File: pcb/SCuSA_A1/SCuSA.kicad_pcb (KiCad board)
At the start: 2 copper layers, 22 parts, among them J101 Header_01x02_Wurth_61300211121, J102 USB4135-GF-A, Q102 DMP2022LSS, U1 LM27762, U101 MCP73812T-420I-OT, U103 BQ297xy

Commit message: Work on battery charger
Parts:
- removed J101: Header_01x02_Wurth_61300211121, Connector_PinHeader_2.54mm:PinHeader_1x02_P2.54mm_Vertical
- added D101: 150080SS75000, LED_SMD:LED_0805_2012Metric_Pad1.15x1.40mm_HandSolder, F.Cu at (143.7, 78.4)
- added F101: 0ZCJ0110FF2E, Fuse:Fuse_1206_3216Metric_Pad1.42x1.75mm_HandSolder, F.Cu at (144.2, 75.2)
- added J105: JST_S2B-PH-K-x, Connector_JST:JST_PH_S2B-PH-K_1x02_P2.00mm_Horizontal, F.Cu at (144.2, 66.3)
- added R109: 5.1M,0603, Resistor_SMD:R_0603_1608Metric_Pad0.98x0.95mm_HandSolder, F.Cu at (139.1, 65.2)
- added R110: 5.1M,0603, Resistor_SMD:R_0603_1608Metric_Pad0.98x0.95mm_HandSolder, F.Cu at (139.1, 67.7)
- added R111: 5.1k,0603, Resistor_SMD:R_0603_1608Metric_Pad0.98x0.95mm_HandSolder, F.Cu at (139.1, 70.2)
- added R112: 5.1k,0603, Resistor_SMD:R_0603_1608Metric_Pad0.98x0.95mm_HandSolder, F.Cu at (139.1, 72.7)
- added R113: 10k,0603, Resistor_SMD:R_0603_1608Metric_Pad0.98x0.95mm_HandSolder, F.Cu at (139.1, 75.2)
- added U104: TLV803EA30DBZR, Package_TO_SOT_SMD:SOT-23, F.Cu at (149.7, 75.8)
- Q102: value DMP2022LSS -> DMN2041LSD
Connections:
- C1 pad 1: VBat -> /VBat_SW
- C104 pad 1: VBat -> /VBat
- J102 pad A5: unconnected-(J102-CC1-PadA5) -> Net-(J102-CC1)
- J102 pad A9: /VBus -> Net-(F101-Pad1)
- J102 pad B5: unconnected-(J102-CC2-PadB5) -> Net-(J102-CC2)
- J102 pad B9: /VBus -> Net-(F101-Pad1)
- R102 pad 1: VBat -> /VBat
- U1 pad 12: unconnected-(U1-EN+-Pad12) -> Net-(JP102-B)
- U1 pad 3: VBat -> /VBat_SW
- U1 pad 8: unconnected-(U1-EN--Pad8) -> Net-(JP101-B)
- U101 pad 3: VBat -> /VBat
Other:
- board outline added: 40 x 30 mm

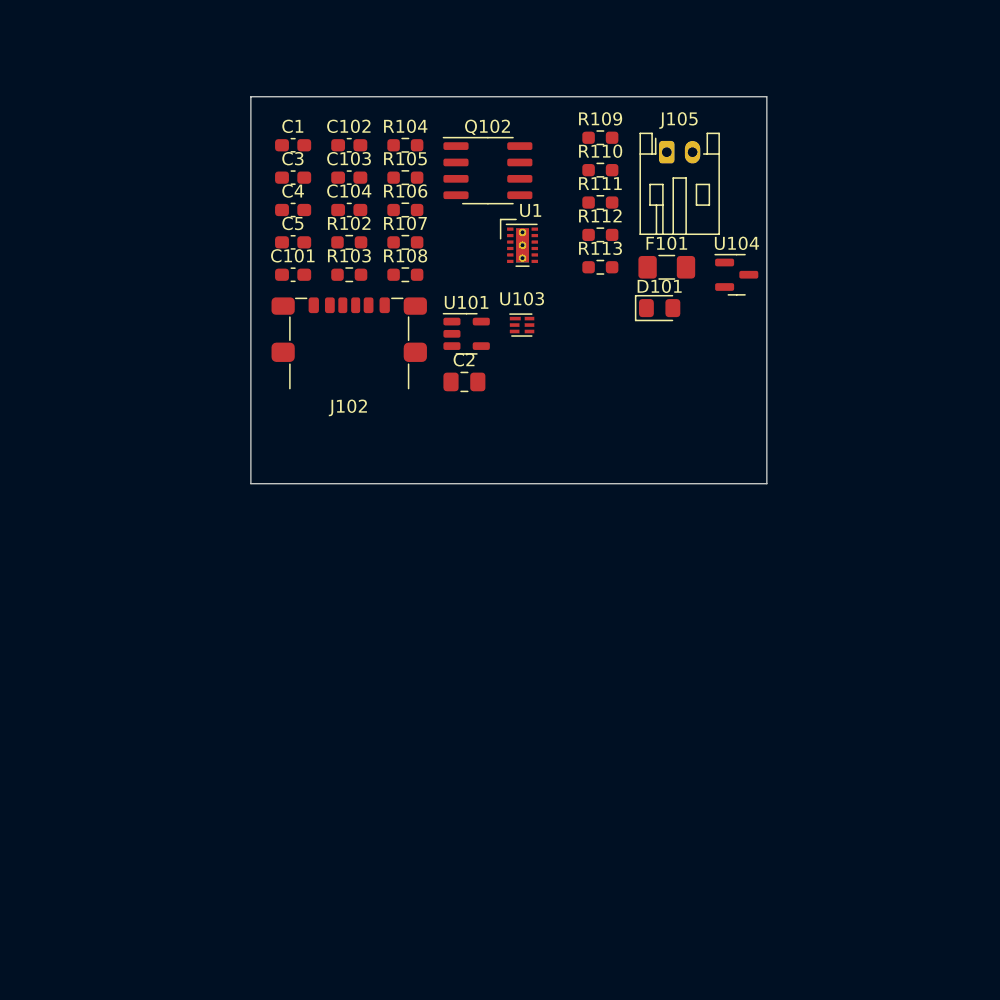
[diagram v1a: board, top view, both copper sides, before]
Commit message: Add trimpot, bindingpost
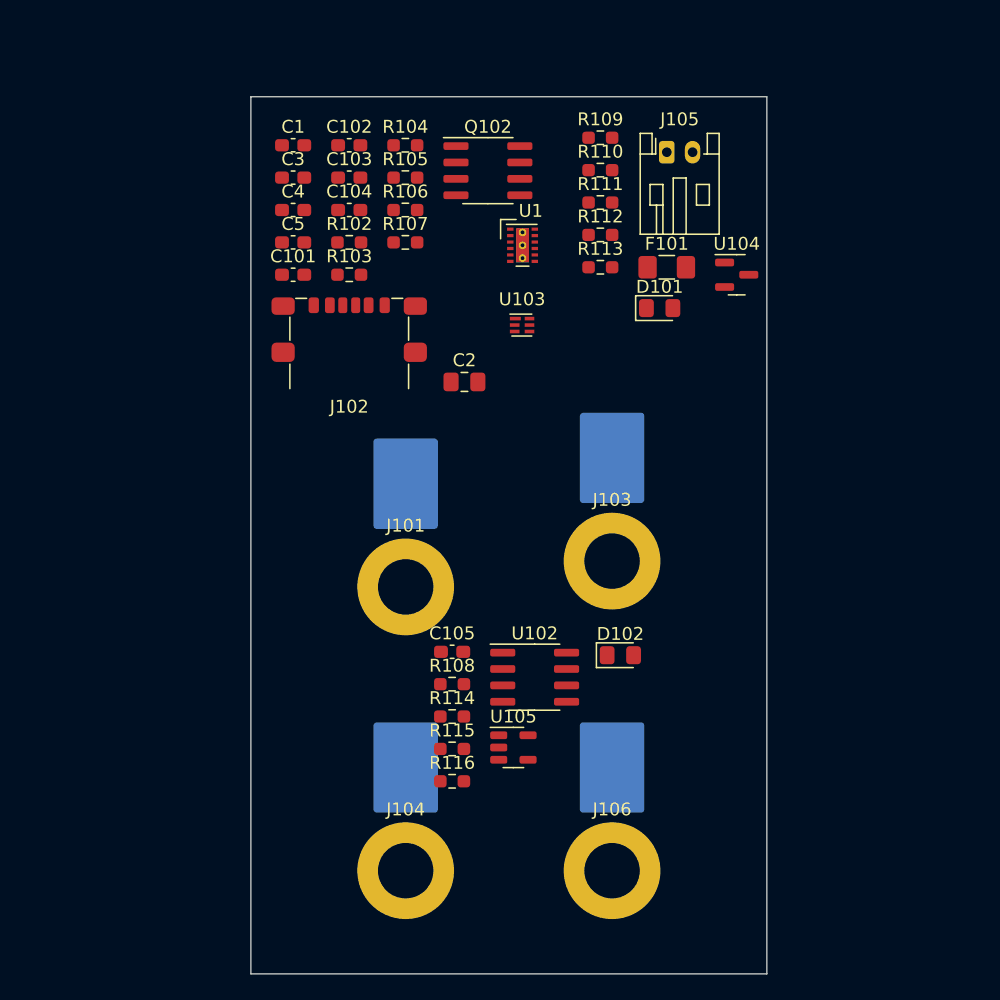
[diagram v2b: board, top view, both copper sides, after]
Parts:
- removed U101: MCP73812T-420I-OT, Package_TO_SOT_SMD:SOT-23-5
- added C105: 100nF,100V,X7R,0603, Capacitor_SMD:C_0603_1608Metric_Pad1.08x0.95mm_HandSolder, F.Cu at (127.6, 105.0)
- added D102: 150080BS75000, LED_SMD:LED_0805_2012Metric_Pad1.15x1.40mm_HandSolder, F.Cu at (140.6, 105.3)
- added J101: Binding_Post_PK4_Red, Connector_User:Binding_Post_4.3mm_M4_DIN965_Pad, F.Cu at (124.0, 100.0)
- added J103: Binding_Post_PK4_Black, Connector_User:Binding_Post_4.3mm_M4_DIN965_Pad, F.Cu at (140.0, 98.0)
- added J104: Binding_Post_PK4_Black, Connector_User:Binding_Post_4.3mm_M4_DIN965_Pad, F.Cu at (124.0, 122.0)
- added J106: Binding_Post_PK4_Red, Connector_User:Binding_Post_4.3mm_M4_DIN965_Pad, F.Cu at (140.0, 122.0)
- added R114: 470R,0603, Resistor_SMD:R_0603_1608Metric_Pad0.98x0.95mm_HandSolder, F.Cu at (127.6, 110.0)
- added R115: 0R,0603, Resistor_SMD:R_0603_1608Metric_Pad0.98x0.95mm_HandSolder, F.Cu at (127.6, 112.6)
- added R116: 0R,0603, Resistor_SMD:R_0603_1608Metric_Pad0.98x0.95mm_HandSolder, F.Cu at (127.6, 115.1)
- added U102: AD8410AWBRZ, Package_SO:SOIC-8_3.9x4.9mm_P1.27mm, F.Cu at (134.0, 107.0)
- added U105: MCP73832T-2ACI/OT, Package_TO_SOT_SMD:SOT-23-5, F.Cu at (132.3, 112.5)
- R108: value 10k,0603 -> 2k,0603
- moved R108 31.9 mm to (127.6, 107.5)
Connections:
- net Net-(U1-OUT-) renamed /-2V
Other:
- board size 40 x 30 mm -> 40 x 68 mm

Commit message: Completion of schematic (for now)
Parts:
- removed C1, C3, C4: 2.2uF,25V,X7R,0603, Capacitor_SMD:C_0603_1608Metric_Pad1.08x0.95mm_HandSolder
- removed C2: 4.7uF,25V,X7R,0805, Capacitor_SMD:C_0805_2012Metric_Pad1.18x1.45mm_HandSolder
- removed C5: 470nF,25V,X7R,0603, Capacitor_SMD:C_0603_1608Metric_Pad1.08x0.95mm_HandSolder
- removed Q102: DMN2041LSD, Package_SO:SOIC-8_3.9x4.9mm_P1.27mm
- removed U1: LM27762, Package_SON:WSON-12-1EP_3x2mm_P0.5mm_EP1x2.65_ThermalVias
- added C106: 470nF,25V,X7R,0603, Capacitor_SMD:C_0603_1608Metric_Pad1.08x0.95mm_HandSolder, F.Cu at (129.8, 93.8)
- added C107: 2.2uF,25V,X7R,0603, Capacitor_SMD:C_0603_1608Metric_Pad1.08x0.95mm_HandSolder, F.Cu at (129.8, 96.3)
- added C108: 4.7uF,25V,X7R,0805, Capacitor_SMD:C_0805_2012Metric_Pad1.18x1.45mm_HandSolder, F.Cu at (142.4, 125.1)
- added C109: 100nF,100V,X7R,0603, Capacitor_SMD:C_0603_1608Metric_Pad1.08x0.95mm_HandSolder, F.Cu at (134.1, 81.2)
- added C110: 100nF,100V,X7R,0603, Capacitor_SMD:C_0603_1608Metric_Pad1.08x0.95mm_HandSolder, F.Cu at (134.1, 83.7)
- added C111: 100nF,100V,X7R,0603, Capacitor_SMD:C_0603_1608Metric_Pad1.08x0.95mm_HandSolder, F.Cu at (134.1, 86.2)
- added C112: 100nF,16V,X7R,0603, Capacitor_SMD:C_0603_1608Metric_Pad1.08x0.95mm_HandSolder, F.Cu at (134.1, 88.8)
- added D103: 150080SS75000, LED_SMD:LED_0805_2012Metric_Pad1.15x1.40mm_HandSolder, F.Cu at (131.7, 124.3)
- added JP101: SolderJumper_2_Bridged, Jumper:SolderJumper-2_P1.3mm_Bridged_Pad1.0x1.5mm, F.Cu at (136.3, 118.5)
- added JP102: SolderJumper_2_Bridged, Jumper:SolderJumper-2_P1.3mm_Bridged_Pad1.0x1.5mm, F.Cu at (136.3, 122.0)
- added JP103: SolderJumper_3_Bridged12, Jumper:SolderJumper-3_P1.3mm_Bridged12_Pad1.0x1.5mm_NumberLabels, F.Cu at (148.8, 122.0)
- added Q101: DMN2041LSD, Package_SO:SOIC-8_3.9x4.9mm_P1.27mm, F.Cu at (149.2, 91.3)
- added R101: 5.1k,0603, Resistor_SMD:R_0603_1608Metric_Pad0.98x0.95mm_HandSolder, F.Cu at (134.1, 91.3)
- added R117: 10k,0603, Resistor_SMD:R_0603_1608Metric_Pad0.98x0.95mm_HandSolder, F.Cu at (142.8, 93.8)
- added RV101: 10k_Potentiometer_Trim_TSR-3296W, Potentionmeter_THT_User:Potentiometer_Suntan_3296W_Vertical, F.Cu at (148.1, 107.4)
- added SW101: JS202011CQN, Button_Switch_THT:SW_CuK_JS202011CQN_DPDT_Straight, F.Cu at (132.3, 105.7)
- added SW102: JS202011CQN, Button_Switch_THT:SW_CuK_JS202011CQN_DPDT_Straight, F.Cu at (132.3, 111.9)
- added U101: MCP73832T-2ACI/OT, Package_TO_SOT_SMD:SOT-23-5, F.Cu at (135.8, 99.8)
- C101, C102: value 100nF,16V,X7R,0603 -> 1uF,16V,X7R,0603
- C103: value 1uF,16V,X7R,0603 -> 100nF,16V,X7R,0603
- C104: value 1uF,16V,X7R,0603 -> 2.2uF,25V,X7R,0603
- C105: value 100nF,100V,X7R,0603 -> 2.2uF,25V,X7R,0603
- D101: value 150080SS75000 -> 150080BS75000
- D102: value 150080BS75000 -> 150080SS75000
- J101: value Binding_Post_PK4_Red -> USB4135-GF-A; footprint Connector_User:Binding_Post_4.3mm_M4_DIN965_Pad -> Connector_User:USB-C_Receptacle_GTC_USB4135-GF-A
- J102: value USB4135-GF-A -> JST_S2B-PH-K-x; footprint Connector_User:USB-C_Receptacle_GTC_USB4135-GF-A -> Connector_JST:JST_PH_S2B-PH-K_1x02_P2.00mm_Horizontal
- J103: value Binding_Post_PK4_Black -> Binding_Post_PK4_Red
- J105: value JST_S2B-PH-K-x -> Binding_Post_PK4_Red; footprint Connector_JST:JST_PH_S2B-PH-K_1x02_P2.00mm_Horizontal -> Connector_User:Binding_Post_4.3mm_M4_DIN965_Pad
- J106: value Binding_Post_PK4_Red -> Binding_Post_PK4_Black
- R102: value 330R,0603 -> 5.1k,0603
- R103: value 120k,0603 -> 2k,0603
- R104: value 68k,0603 -> 470R,0603
- R105: value 120k,0603 -> 330R,0603
- R106: value 68k,0603 -> 2.2k,0603
- R107: value 2.2k,0603 -> 5.1M,0603
- R108: value 2k,0603 -> 5.1M,0603
- R109: value 5.1M,0603 -> 10k,0603
- R110: value 5.1M,0603 -> 120k,0603
- R111, R112: value 5.1k,0603 -> 68k,0603
- R113: value 10k,0603 -> 120k,0603
- R114: value 470R,0603 -> 50m; footprint Resistor_SMD:R_0603_1608Metric_Pad0.98x0.95mm_HandSolder -> Resistor_SMD:R_1206_3216Metric
- U102: value AD8410AWBRZ -> BQ297xy; footprint Package_SO:SOIC-8_3.9x4.9mm_P1.27mm -> Package_SON:WSON-6_1.5x1.5mm_P0.5mm
- U103: value BQ297xy -> TLV803EA30DBZR; footprint Package_SON:WSON-6_1.5x1.5mm_P0.5mm -> Package_TO_SOT_SMD:SOT-23
- U104: value TLV803EA30DBZR -> LM27762; footprint Package_TO_SOT_SMD:SOT-23 -> Package_SON:WSON-12-1EP_3x2mm_P0.5mm_EP1x2.65_ThermalVias
- U105: value MCP73832T-2ACI/OT -> AD8410AWBRZ; footprint Package_TO_SOT_SMD:SOT-23-5 -> Package_SO:SOIC-8_3.9x4.9mm_P1.27mm
- moved J104 64.6 mm to (161.0, 69.0)
- moved J105 62.1 mm to (119.0, 123.0)
- moved F101 46.7 mm to (143.0, 121.9)
- moved J102 41.9 mm to (143.0, 113.0)
- moved D101 41.6 mm to (131.7, 118.2)
- moved U104 37.4 mm to (150.2, 113.2)
- moved J103 36.6 mm to (119.0, 68.0)
- moved J101 33.4 mm to (151.5, 81.2)
- moved R110 28.6 mm to (138.5, 96.3)
- moved R109 28.6 mm to (138.5, 93.8)
- moved R115 28.2 mm to (142.8, 88.8)
- moved R116 28.2 mm to (142.8, 91.3)
- moved R103 25.1 mm to (134.1, 96.3)
- moved R102 25.1 mm to (134.1, 93.8)
- moved U105 22.3 mm to (149.2, 97.8)
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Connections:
- C101 pad 1: +3V3 -> /VBus
- C102 pad 1: Net-(U103-BAT) -> /VBat
- C102 pad 2: /Cell- -> GND
- C103 pad 1: /VBus -> Net-(U102-BAT)
- C103 pad 2: GND -> /Cell-
- C104 pad 1: /VBat -> /VBat_SW
- C105 pad 1: Net-(U102-IN+) -> +3V3
- C105 pad 2: Net-(U102-IN-) -> GND
- J104 pad 1: GND -> Net-(J104-Pad1)
- J105 pad 1: /VBat -> Net-(U105-OUT)
- J106 pad 1: Net-(U102-OUT) -> GND
- R102 pad 1: /VBat -> Net-(J101-CC2)
- R102 pad 2: Net-(U103-BAT) -> GND
- R103 pad 1: +3V3 -> Net-(U101-PROG)
- R103 pad 2: Net-(U1-FB+) -> GND
- R104 pad 1: Net-(U1-FB+) -> /VBus
- R104 pad 2: GND -> Net-(D101-A)
- R105 pad 1: Net-(U1-FB-) -> /VBat
- R105 pad 2: /-2V -> Net-(U102-BAT)
- R106 pad 1: GND -> Net-(U102-V-)
- R106 pad 2: Net-(U1-FB-) -> GND
- R107 pad 1: Net-(U103-V-) -> Net-(Q101A-G1)
- R108 pad 1: Net-(U105-PROG) -> Net-(Q101B-G2)
- R108 pad 2: GND -> /Cell-
- R109 pad 1: Net-(Q102B-G2) -> /VBat_SW
- R109 pad 2: /Cell- -> Net-(D102-A)
- R110 pad 1: Net-(Q102A-G1) -> +3V3
- R110 pad 2: GND -> Net-(U104-FB+)
- R111 pad 1: Net-(J102-CC1) -> Net-(U104-FB+)
- R112 pad 1: Net-(J102-CC2) -> GND
- R112 pad 2: GND -> Net-(U104-FB-)
- R113 pad 1: /VBat_SW -> Net-(U104-FB-)
- R113 pad 2: Net-(D101-A) -> /-2V
- R114 pad 1: /VBus -> Net-(J103-Pad1)
- R114 pad 2: Net-(D102-A) -> Net-(J104-Pad1)
- R115 pad 2: Net-(U102-IN-) -> Net-(U105-IN+)
- R116 pad 1: Net-(J101-Pad1) -> Net-(J104-Pad1)
- R116 pad 2: Net-(U102-IN+) -> Net-(U105-IN-)
- U102 pad 1: Net-(U102-IN-) -> unconnected-(U102-NC-Pad1)
- U102 pad 2: Net-(U102-GND) -> Net-(Q101A-G1)
- U102 pad 3: Net-(SW101B-B) -> Net-(Q101B-G2)
- U102 pad 4: unconnected-(U102-NC-Pad4) -> /Cell-
- U102 pad 5: Net-(U102-OUT) -> Net-(U102-BAT)
- U102 pad 6: +3V3 -> Net-(U102-V-)
- U103 pad 1: unconnected-(U103-NC-Pad1) -> GND
- U103 pad 2: Net-(Q102A-G1) -> Net-(D102-K)
- U103 pad 3: Net-(Q102B-G2) -> /VBat_SW
- U104 pad 1: GND -> /PGOOD
- U104 pad 2: Net-(D101-K) -> Net-(U104-FB+)
- U105 pad 1: Net-(D102-K) -> Net-(U105-IN-)
- U105 pad 2: GND -> -VOffset
- U105 pad 3: /VBat -> Net-(SW102B-B)
- U105 pad 4: /VBus -> unconnected-(U105-NC-Pad4)
- U105 pad 5: Net-(U105-PROG) -> Net-(U105-OUT)
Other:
- board size 40 x 68 mm -> 56 x 68 mm

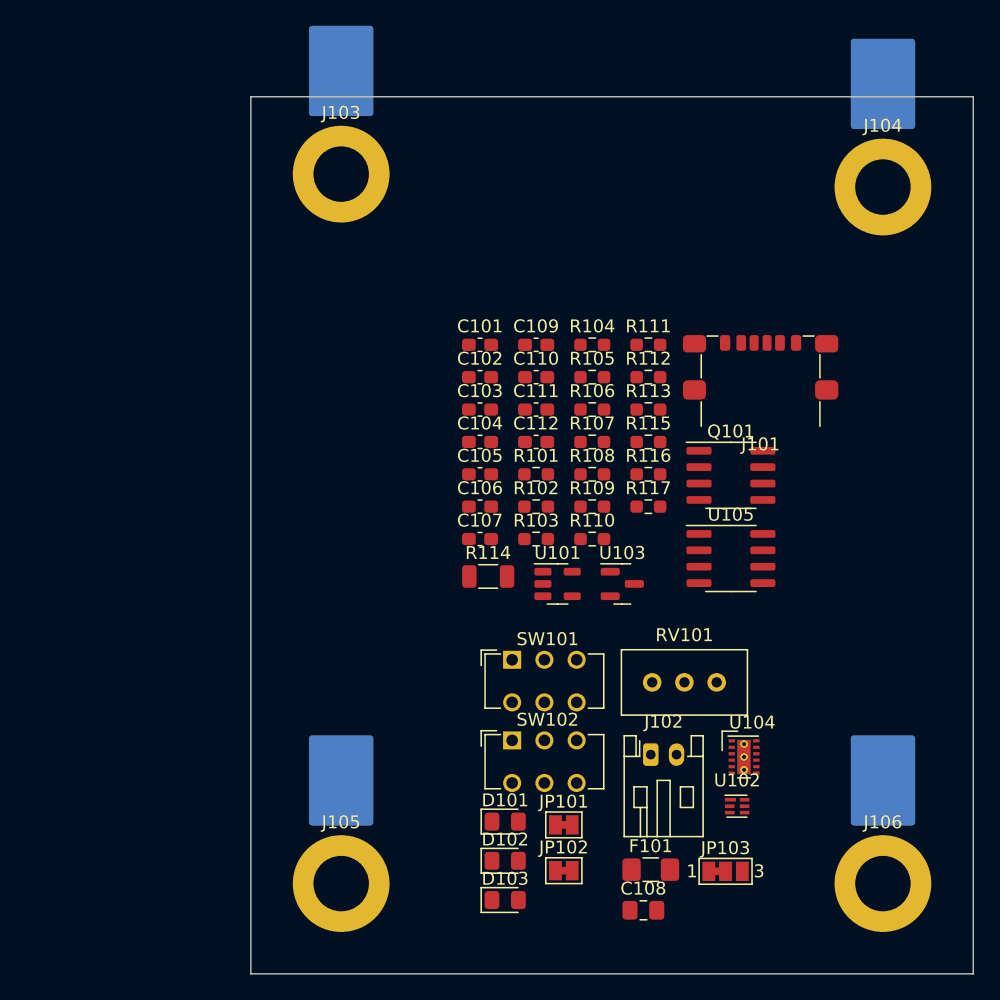
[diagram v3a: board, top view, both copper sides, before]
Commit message: Add connectors, supply voltage filter
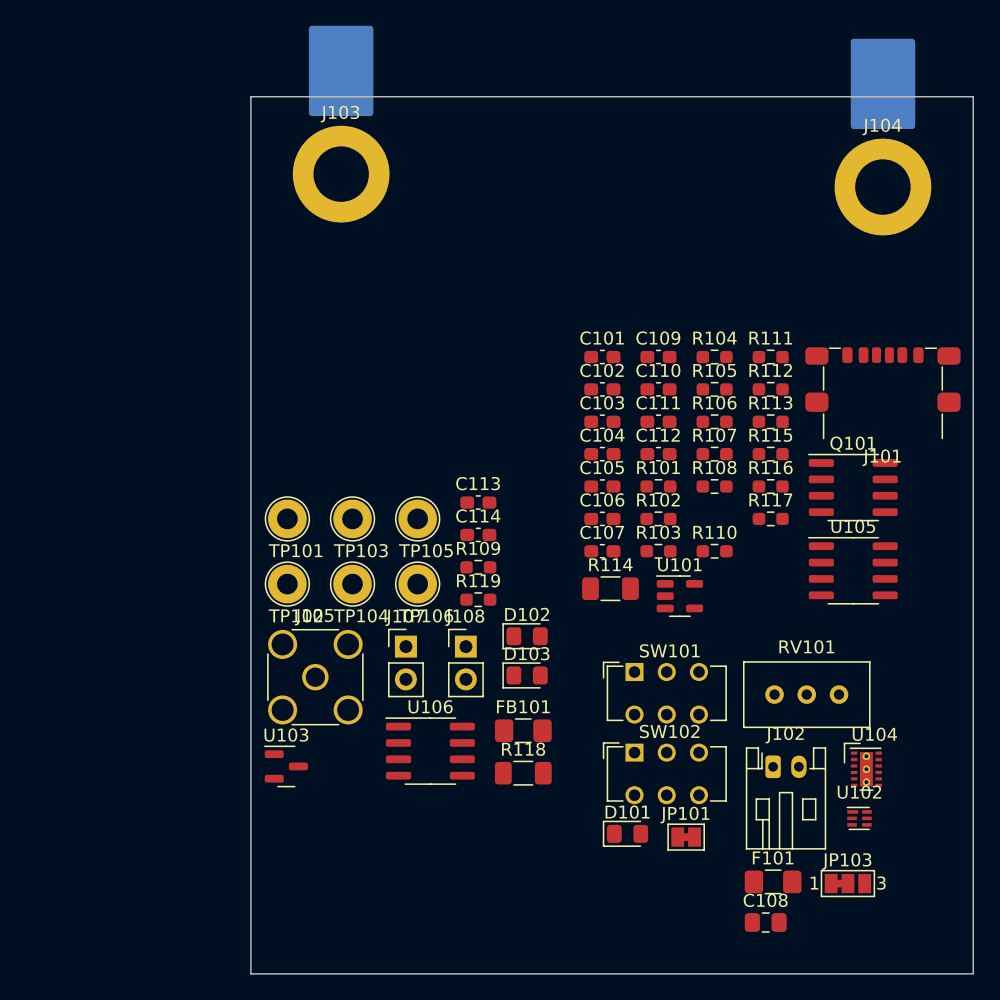
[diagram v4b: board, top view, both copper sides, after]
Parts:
- removed J106: Binding_Post_PK4_Black, Connector_User:Binding_Post_4.3mm_M4_DIN965_Pad
- removed JP102: SolderJumper_2_Bridged, Jumper:SolderJumper-2_P1.3mm_Bridged_Pad1.0x1.5mm
- added C113: 100nF,16V,X7R,0603, Capacitor_SMD:C_0603_1608Metric_Pad1.08x0.95mm_HandSolder, F.Cu at (129.6, 93.5)
- added C114: 1uF,16V,X7R,0603, Capacitor_SMD:C_0603_1608Metric_Pad1.08x0.95mm_HandSolder, F.Cu at (129.6, 96.0)
- added FB101: 742792620, Inductor_SMD:L_1206_3216Metric_Pad1.42x1.75mm_HandSolder, F.Cu at (133.1, 111.2)
- added J107: 77311-118-02LF, Connector_PinHeader_2.54mm:PinHeader_1x02_P2.54mm_Vertical, F.Cu at (124.0, 104.6)
- added J108: 77311-118-02LF, Connector_PinHeader_2.54mm:PinHeader_1x02_P2.54mm_Vertical, F.Cu at (128.7, 104.6)
- added R118: 49.9R,1206, Resistor_SMD:R_1206_3216Metric_Pad1.30x1.75mm_HandSolder, F.Cu at (133.1, 114.4)
- added R119: 0R,0603, Resistor_SMD:R_0603_1608Metric_Pad0.98x0.95mm_HandSolder, F.Cu at (129.6, 101.0)
- added TP101: TestPoint_5010_Red, TestPoint:TestPoint_Loop_D2.60mm_Drill1.6mm_Beaded, F.Cu at (114.8, 94.7)
- added TP102: TestPoint_5011_Black, TestPoint:TestPoint_Loop_D2.60mm_Drill1.6mm_Beaded, F.Cu at (114.8, 99.8)
- added TP103: TestPoint_5010_Red, TestPoint:TestPoint_Loop_D2.60mm_Drill1.6mm_Beaded, F.Cu at (119.9, 94.7)
- added TP104: TestPoint_5011_Black, TestPoint:TestPoint_Loop_D2.60mm_Drill1.6mm_Beaded, F.Cu at (119.9, 99.8)
- added TP105: TestPoint_5010_Red, TestPoint:TestPoint_Loop_D2.60mm_Drill1.6mm_Beaded, F.Cu at (124.9, 94.7)
- added TP106: TestPoint_5012_White, TestPoint:TestPoint_Loop_D2.60mm_Drill1.6mm_Beaded, F.Cu at (124.9, 99.8)
- added U106: AD8655ARZ, Package_SO:SOIC-8_3.9x4.9mm_P1.27mm, F.Cu at (125.9, 112.7)
- D103: value 150080SS75000 -> 150080GS75000
- J105: value Binding_Post_PK4_Red -> SMA_Straight_Jack_Female; footprint Connector_User:Binding_Post_4.3mm_M4_DIN965_Pad -> Connector_Coaxial:SMA_Wurth_60312002114503_Vertical
- R114: footprint Resistor_SMD:R_1206_3216Metric -> Resistor_SMD:R_1206_3216Metric_Pad1.30x1.75mm_HandSolder
- moved U103 29.6 mm to (114.8, 113.9)
- moved D103 17.5 mm to (133.4, 106.9)
- moved D102 17.5 mm to (133.4, 103.8)
- moved J105 16.1 mm to (117.0, 107.0)
- moved R109 10.0 mm to (129.6, 98.5)
- moved C102 9.53 mm to (139.2, 84.7)
- moved C103 9.53 mm to (139.2, 87.2)
- moved C105 9.53 mm to (139.2, 92.2)
- moved C106 9.53 mm to (139.2, 94.7)
- moved F101 9.53 mm to (152.5, 122.9)
- moved J102 9.53 mm to (152.5, 113.9)
- moved R112 9.53 mm to (152.3, 84.7)
- moved R113 9.53 mm to (152.3, 87.2)
- moved R116 9.53 mm to (152.3, 92.2)
- moved R117 9.53 mm to (152.3, 94.7)
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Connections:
- D103 pad 1: GND -> /PGOOD
- D103 pad 2: /PGOOD -> Net-(D103-A)
- J105 pad 1: Net-(U105-OUT) -> Net-(J105-In)
- JP103 pad 1: /-2V -> /-2V_filt
- R117 pad 1: /PGOOD -> Net-(D103-A)
- U105 pad 5: Net-(U105-OUT) -> /Out

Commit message: Preliminary BOM
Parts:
- C106: value 470nF,25V,X7R,0603 -> 1uF,16V,X7R,0603
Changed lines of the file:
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@@
         (effects (font (size 1 1) (thickness 0.15)))
     )
-    (fp_text value "470nF,25V,X7R,0603" (at 0 1.43) (layer "F.Fab")
+    (fp_text value "1uF,16V,X7R,0603" (at 0 1.43) (layer "F.Fab")
         (effects (font (size 1 1) (thickness 0.15)))
     )

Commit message: Work on PCB layout
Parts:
- added TP107: TestPoint_5011_Black, TestPoint:TestPoint_Loop_D2.60mm_Drill1.6mm_Beaded, F.Cu at (147.5, 120.0)
- added TP108: TestPoint_5010_Red, TestPoint:TestPoint_Loop_D2.60mm_Drill1.6mm_Beaded, F.Cu at (147.5, 125.0)
- J102: moved to B.Cu
- J103: footprint Connector_User:Binding_Post_4.3mm_M4_DIN965_Pad -> Connector_User:Binding_Post_PK4_Red
- J104: footprint Connector_User:Binding_Post_4.3mm_M4_DIN965_Pad -> Connector_User:Binding_Post_PK4_Black
- J105: footprint Connector_Coaxial:SMA_Wurth_60312002114503_Vertical -> Connector_User:SMA_Vertical
- R113: value 120k,0603 -> 47k,0603
- RV101: footprint Potentionmeter_THT_User:Potentiometer_Suntan_3296W_Vertical -> Potentionmeter_THT_User:Potentiometer_Suntan_3296W_Vertical_90deg
- U102: value BQ297xy -> BQ29700DSER
- moved J102 54.5 mm to (117.0, 72.5), turned to 180 degrees
- moved U102 52.1 mm to (121.0, 82.5), turned to 90 degrees
- moved J101 48.5 mm to (120.0, 108.1)
- moved Q101 43.6 mm to (116.0, 83.5), turned to -90 degrees
- moved R104 35.2 mm to (117.0, 98.9), turned to 90 degrees
- moved J104 35.0 mm to (126.0, 69.0), turned to 180 degrees
- moved D101 34.9 mm to (116.5, 94.5), turned to -90 degrees
- moved F101 34.6 mm to (123.5, 104.0), turned to 90 degrees
- moved R107 34.3 mm to (129.0, 118.3)
- moved R106 34.3 mm to (129.0, 115.8)
- moved R108 34.3 mm to (129.0, 120.8)
- moved R114 31.3 mm to (137.0, 69.0), turned to 180 degrees
- moved J108 30.0 mm to (156.9, 94.5), turned to 90 degrees
- moved J103 29.0 mm to (148.0, 69.0), turned to 180 degrees
- moved U105 29.0 mm to (137.0, 79.5)
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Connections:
- C112 pad 2: GND -> -VOffset
